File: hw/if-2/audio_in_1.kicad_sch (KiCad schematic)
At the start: 32 parts, among them U61 TL072, U62 TL072

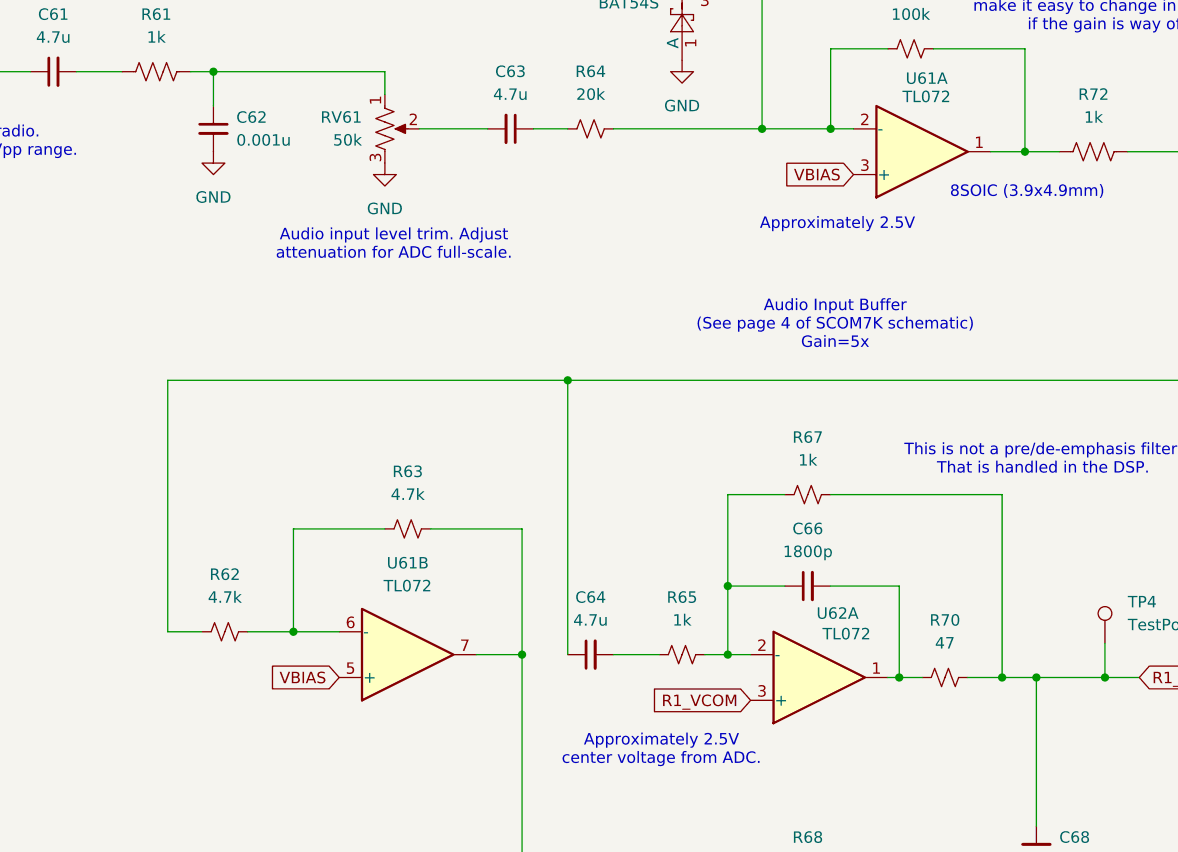
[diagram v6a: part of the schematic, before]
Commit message: (Pre fab) Resolved warning with DB25 shell connections to ground
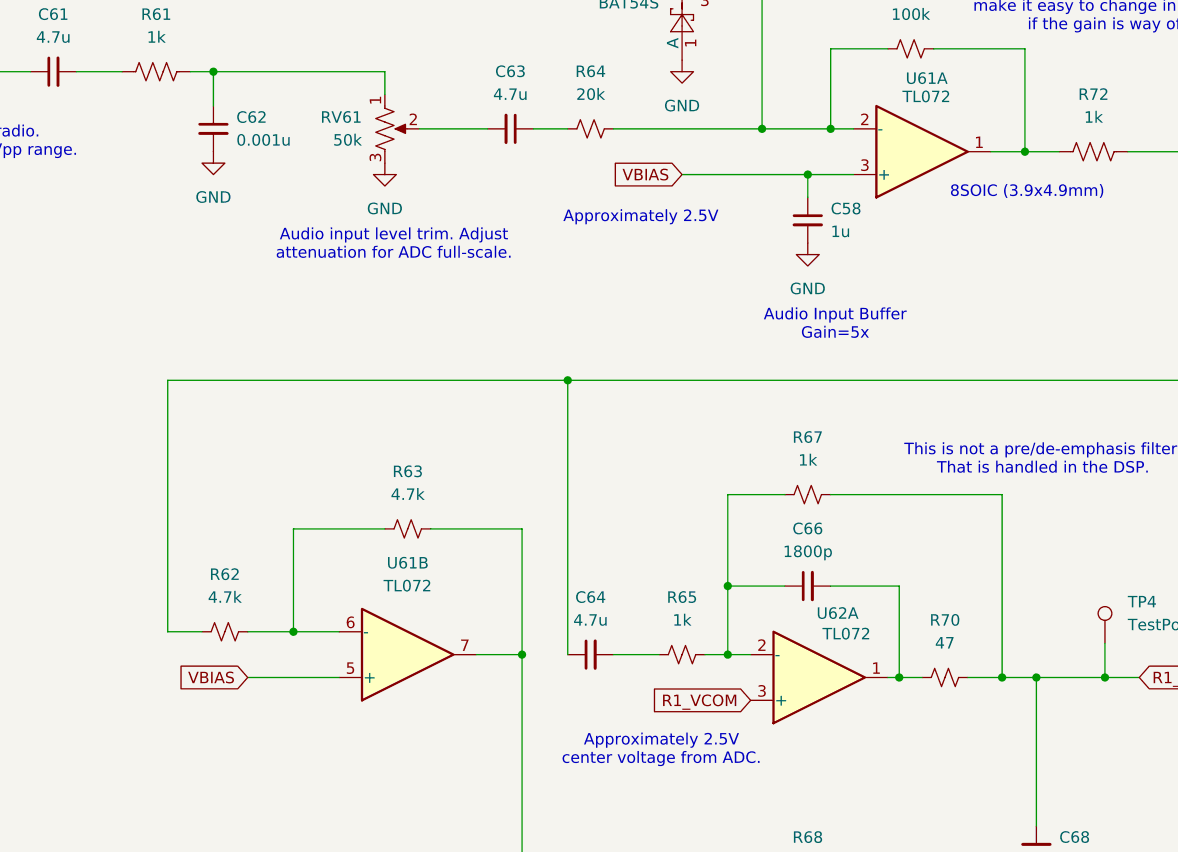
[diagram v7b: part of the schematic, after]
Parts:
- added C58: 1u, Capacitor_SMD:C_0805_2012Metric_Pad1.18x1.45mm_HandSolder, symbol Device:C_Small
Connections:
- net GND: now also C58.2
- net VBIAS: now also C58.1
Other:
- note added: "Audio Input Buffer Gain=5x"
- note removed: "Audio Input Buffer (See page 4 of SCOM7K schematic) Gain=5x"
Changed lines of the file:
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@@
 	(text "Approximately 2.5V\n"
 		(exclude_from_sim no)
-		(at 141.732 55.118 0)
+		(at 119.888 54.356 0)
 		(effects
 			(font
@@
 		)
 	)
-	(text "Audio Input Buffer\n(See page 4 of SCOM7K schematic)\nGain=5x"
+	(text "Audio Input Buffer\nGain=5x"
 		(exclude_from_sim no)
 		(at 141.478 66.294 0)
@@
 	)
 	(junction
+		(at 138.43 49.53)
+		(diameter 0)
+		(color 0 0 0 0)
+	)
+	(junction
 		(at 129.54 102.87)
 		(diameter 0)
@@
 	(wire
 		(pts
+			(xy 76.2 105.41) (xy 86.36 105.41)
+		)
+		(stroke
+			(width 0)
+			(type default)
+		)
+	)
+	(wire
+		(pts
 			(xy 72.39 38.1) (xy 91.44 38.1)
 		)
@@
 	(wire
 		(pts
+			(xy 124.46 49.53) (xy 138.43 49.53)
+		)
+		(stroke
+			(width 0)
+			(type default)
+		)
+	)
+	(wire
+		(pts
+			(xy 138.43 49.53) (xy 143.51 49.53)
+		)
+		(stroke
+			(width 0)
+			(type default)
+		)
+	)
+	(wire
+		(pts
 			(xy 162.56 35.56) (xy 162.56 46.99)
 		)
@@
 		)
 	)
+	(wire
+		(pts
+			(xy 138.43 49.53) (xy 138.43 52.07)
+		)
+		(stroke
+			(width 0)
+			(type default)
+		)
+	)
 	(global_label "R1_AUDIO_IN"
 		(shape input)
@@
 	(global_label "VBIAS"
 		(shape input)
-		(at 86.36 105.41 180)
+		(at 76.2 105.41 180)
 		(fields_autoplaced yes)
 		(effects
@@
 		)
 		(property "Intersheetrefs" "${INTERSHEET_REFS}"
-			(at 78.1133 105.41 0)
+			(at 67.9533 105.41 0)
 			(effects
 				(font
@@
 	(global_label "VBIAS"
 		(shape input)
-		(at 143.51 49.53 180)
+		(at 124.46 49.53 180)
 		(fields_autoplaced yes)
 		(effects
@@
 		)
 		(property "Intersheetrefs" "${INTERSHEET_REFS}"
-			(at 135.2633 49.53 0)
+			(at 116.2133 49.53 0)
 			(effects
 				(font
@@
 	(symbol
 		(lib_id "power:GND")
+		(at 138.43 57.15 0)
+		(unit 1)
+		(exclude_from_sim no)
+		(in_bom yes)
+		(on_board yes)
+		(dnp no)
+		(fields_autoplaced yes)
+		(property "Reference" "#PWR0158"
+			(at 138.43 63.5 0)
+			(effects
+				(font
+					(size 1.27 1.27)
+				)
+				(hide yes)
+			)
+		)
+		(property "Value" "GND"
+			(at 138.43 62.23 0)
+			(effects
+				(font
+					(size 1.27 1.27)
+				)
+			)
+		)
+		(property "Footprint" ""
+			(at 138.43 57.15 0)
+			(effects
+				(font
+					(size 1.27 1.27)
+				)
+				(hide yes)
+			)
+		)
+		(property "Datasheet" ""
+			(at 138.43 57.15 0)
+			(effects
+				(font
+					(size 1.27 1.27)
+				)
+				(hide yes)
+			)
+		)
+		(property "Description" "Power symbol creates a global label with name \"GND\" , ground"
+			(at 138.43 57.15 0)
+			(effects
+				(font
+					(size 1.27 1.27)
+				)
+				(hide yes)
+			)
+		)
+		(pin "1"
+		)
+		(instances
+			(project "if-2"
+				(path "/a8c2d6aa-29bb-49bd-a367-0d62a0a32480/bbe47db2-4e3f-4928-a954-056c7fb1570e"
+					(reference "#PWR0158")
+					(unit 1)
+				)
+			)
+		)
+	)
+	(symbol
+		(lib_id "power:GND")
 		(at 220.98 48.26 0)
 		(unit 1)
@@
 					(unit 1)
 				)
+			)
+		)
+	)
+	(symbol
+		(lib_id "Device:C_Small")
+		(at 138.43 54.61 0)
+		(unit 1)
+		(exclude_from_sim no)
+		(in_bom yes)
+		(on_board yes)
+		(dnp no)
+		(fields_autoplaced yes)
+		(property "Reference" "C58"
+			(at 140.97 53.3462 0)
+			(effects
+				(font
+					(size 1.27 1.27)
+				)
+				(justify left)
+			)
+		)
+		(property "Value" "1u"
+			(at 140.97 55.8862 0)
+			(effects
+				(font
+					(size 1.27 1.27)
+				)
+				(justify left)
+			)
+		)
+		(property "Footprint" "Capacitor_SMD:C_0805_2012Metric_Pad1.18x1.45mm_HandSolder"
+			(at 138.43 54.61 0)
+			(effects
+				(font
+					(size 1.27 1.27)
+				)
+				(hide yes)
+			)
+		)
+		(property "Datasheet" "~"
+			(at 138.43 54.61 0)
+			(effects
+				(font
+					(size 1.27 1.27)
+				)
+				(hide yes)
+			)
+		)
+		(property "Description" "Unpolarized capacitor, small symbol"
+			(at 138.43 54.61 0)
+			(effects
+				(font
+					(size 1.27 1.27)
+				)
+				(hide yes)
+			)
+		)
+		(pin "1"
+		)
+		(pin "2"
+		)
+		(instances
+			(project "if-2"
+				(path "/a8c2d6aa-29bb-49bd-a367-0d62a0a32480/bbe47db2-4e3f-4928-a954-056c7fb1570e"
+					(reference "C58")
+					(unit 1)
+				)
